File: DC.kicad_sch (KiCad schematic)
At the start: 52 parts, among them J1 348302001, J2 348302001, U6 MCP2551-I-P, U7 NUCLEO-F302R8

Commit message: Updated LEDs, buttons and power distribution headers
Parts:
- added D2: LTST-C193TBKT-5A, LTST-C193TBKT-5A:0603, symbol LTST-C193TBKT-5A:LTST-C193TBKT-5A
- added D3: LTW-C191DS5, LTW-C191DS5:LEDC1608X65N, symbol LTW-C191DS5:LTW-C191DS5
- added F10, F8, F9: 0466.125NR, FUSC3215X66N, symbol 0466_125NR:0466.125NR
- added LED1: LTST-C170GKT, LED_LTST-C170GKT_LTO, symbol 2026-02-10_18-36-51:LTST-C170GKT
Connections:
- net +12V: now also D2.2, D3.A, LED1.2
- net GND: now also U6.5 (Vref), F10.2, F8.2, F9.2
- new net: D3.C, F10.1
- new net: F8.1, LED1.1
- new net: D2.1, F9.1
- no-connect marks 43 -> 42
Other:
- moved on the sheet: J1, J2, a1, a2, a3, a4

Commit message: AccelIn to adc and I2C connection
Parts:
- removed R13: 3.3kΩ, DriverControlsLib:RES-TH_BD2.2-L6.5-P10.50-D0.6, symbol DC_Parts:R
- added D4, D5, D6, D7: LTST-C193TBKT-5A, LTST-C193TBKT-5A:0603, symbol LTST-C193TBKT-5A:LTST-C193TBKT-5A
- added F11, F12, F13, F14, F15, F16, F17, F18: 0466.125NR, FUSC3215X66N, symbol 0466_125NR:0466.125NR
- added J3: 757570141, CONN_SD-75757-010_1X4_F11p20_MOL, symbol 2026-02-11_03-05-32:757570141
- added LED2, LED3, LED4, LED5: LTST-C170GKT, LED_LTST-C170GKT_LTO, symbol 2026-02-10_18-36-51:LTST-C170GKT
- added R18: RC1206FR-07665RL, RC1206FR-07665RL:RESC3116X65N, symbol RC1206FR-07665RL:RC1206FR-07665RL
- added R19, R26, R27, R28, R29: RC1206FR-071K24L, RC1206FR-071K24L:RESC3116X65N, symbol RC1206FR-071K24L:RC1206FR-071K24L
- added R20, R22, R23, R24, R25: RC1206FR-072K32L, RC1206FR-072K32L:RESC3116X65N, symbol RC1206FR-072K32L:RC1206FR-072K32L
- added R21: RC1206FR-102K2L, RC1206FR-102K2L:RESC3116X65N, symbol RC1206FR-102K2L:RC1206FR-102K2L
- added S6, S7, S8, S9: LP6OA2ASRG, LP6OA2ASRG, symbol LP6OA2ASRG:LP6OA2ASRG
- R12: value 12kΩ -> 120Ω
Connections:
- net +12V: now also F10.1, F7.1, F8.1, F9.1, F11.1, F12.1, F13.1, F14.1, F15.1, F16.1, F17.1, F18.1, J3.1; no longer D1.A, D2.2, D3.A, LED1.2
- net +3.3V: now also S6.1, S7.1, S8.1, S9.1
- net AccelIn: now also U7.CN7_28 (PA0); no longer U7.CN10_23 (PA8)
- net CAN_H: now also J3.2
- net CAN_L: now also J3.3
- net GND: now also D1.C, D2.1, D3.C, LED1.1, R12.1, D4.1, D5.1, D6.1, D7.1, J3.4, LED2.1, LED3.1, LED4.1, LED5.1; no longer F10.2, F7.2, F8.2, F9.2, U6.5 (Vref), U6.8 (Rs)
- net SupBattery: no longer R12.1
- net To_PreChargeBtn: now also S4.3; no longer S4.2
- net I2C1_SDA: now reaches U7.CN10_1 (PC9)
- net I2C1_CLK: now reaches U7.CN10_3 (PB8)
- net SupBattMonitor: no longer names the net of R12.2
- net SupBattMonitor: now also U6.8 (Rs); no longer U7.CN10_22 (PB2)
- new net: F10.2, R21.1
- new net: F11.2, R22.1
- new net: D4.2, R22.2
- new net: D3.A, R21.2
- new net: F8.2, R19.1
- new net: F14.2, R25.1
- new net: D7.2, R25.2
- new net: F18.2, R29.1
- new net: F12.2, R23.1
- new net: F15.2, R26.1
- new net: LED2.2, R26.2
- new net: LED1.2, R19.2
- new net: F17.2, R28.1
- new net: LED4.2, R28.2
- new net: D1.A, R18.2
- new net: F7.2, R18.1
- new net: F13.2, R24.1
- new net: D6.2, R24.2
- new net: LED5.2, R29.2
- new net: F16.2, R27.1
- new net: LED3.2, R27.2
- new net: D5.2, R23.2
- new net: F9.2, R20.1
- new net: D2.2, R20.2
- new net SolarBtn: S6.3, S7.3, S8.3, S9.3
- no-connect marks 42 -> 39
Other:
- note removed: "Supplemental Battery Monitor"
- moved on the sheet: C10, C7, C8, C9, D1, D2, D3, F1, F10, F2, F3, F4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

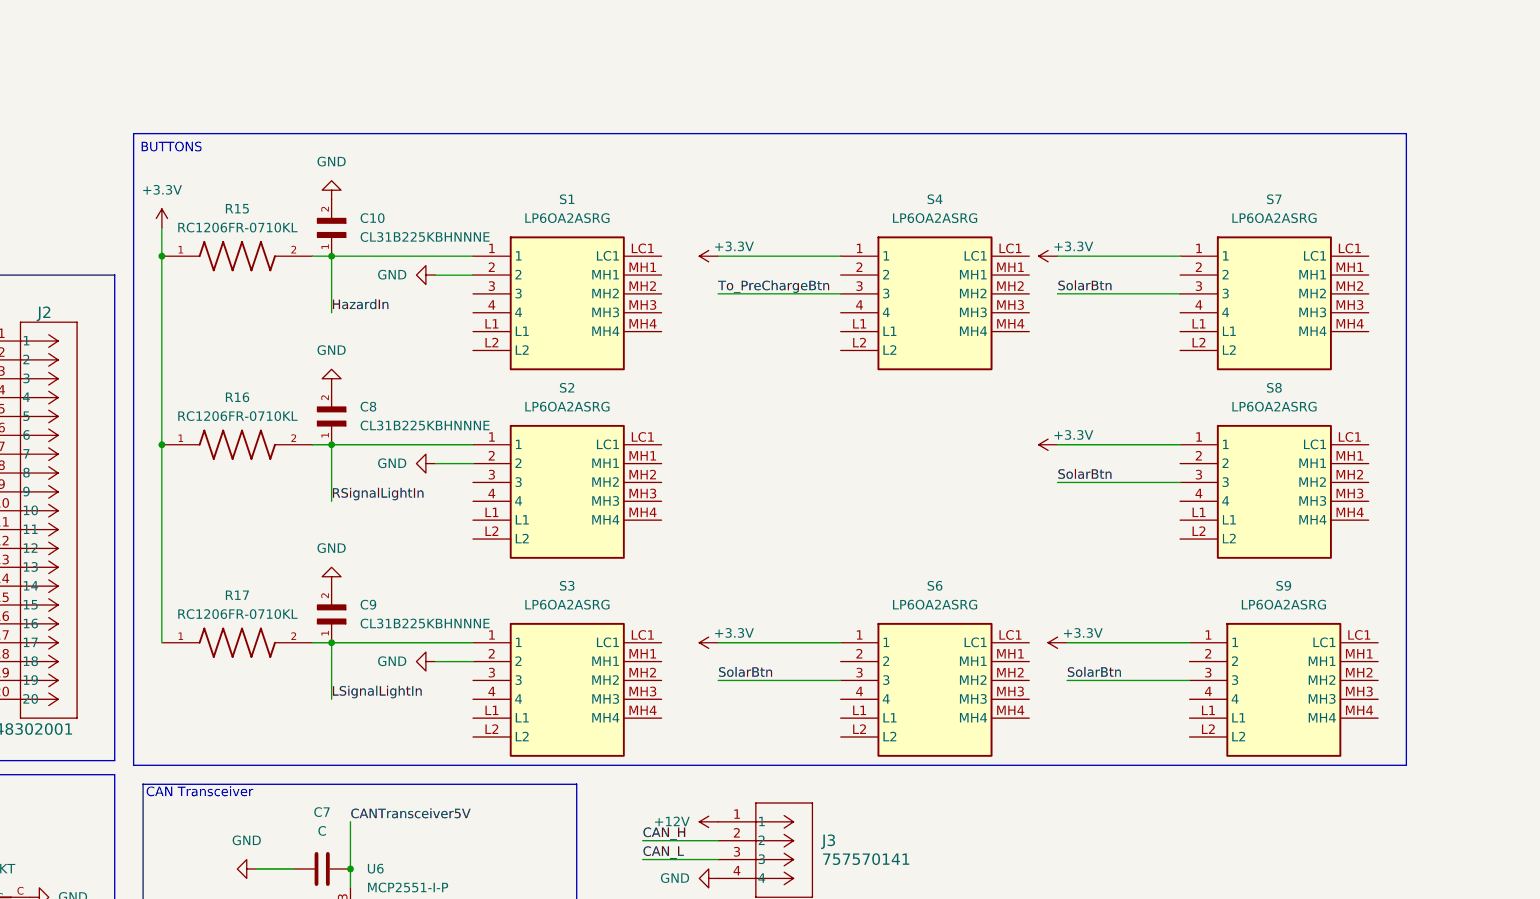
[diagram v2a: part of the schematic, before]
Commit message: Deleted buttons!
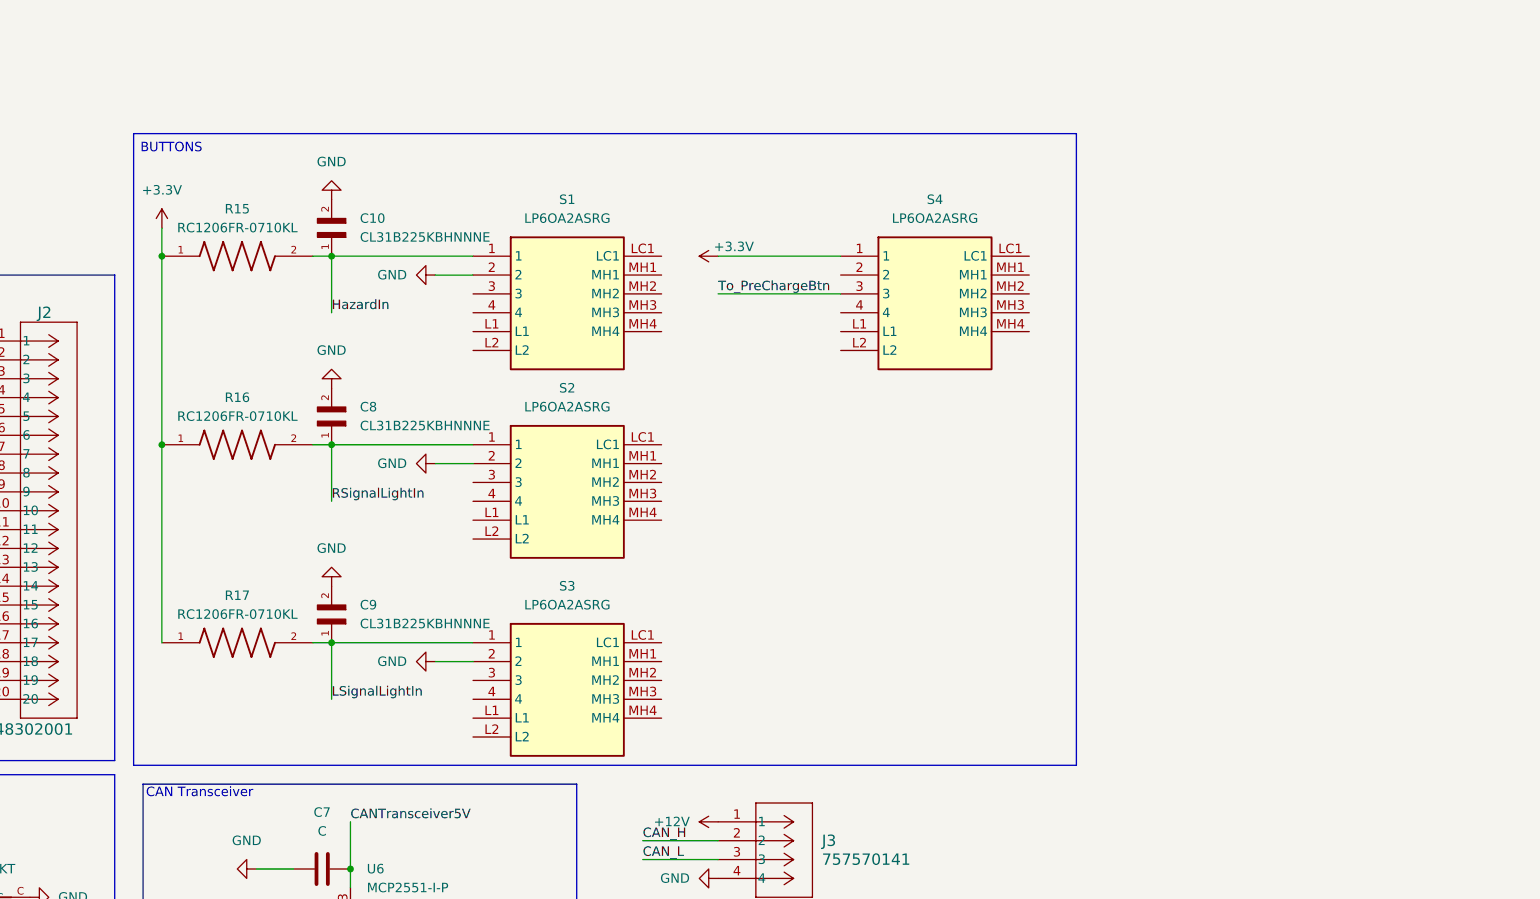
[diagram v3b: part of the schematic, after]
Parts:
- removed S6, S7, S8, S9: LP6OA2ASRG, LP6OA2ASRG, symbol LP6OA2ASRG:LP6OA2ASRG

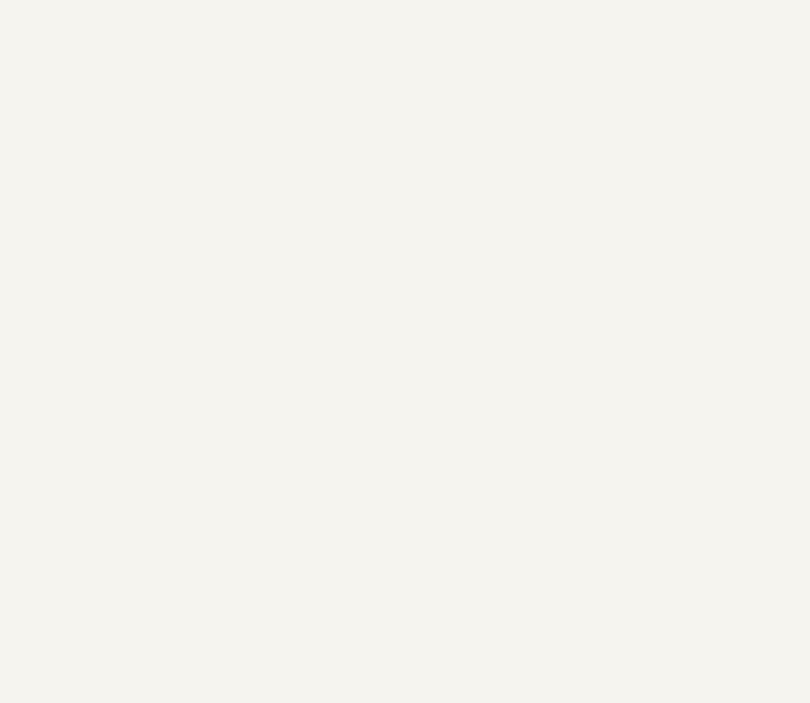
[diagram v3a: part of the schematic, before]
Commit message: Added LCD!
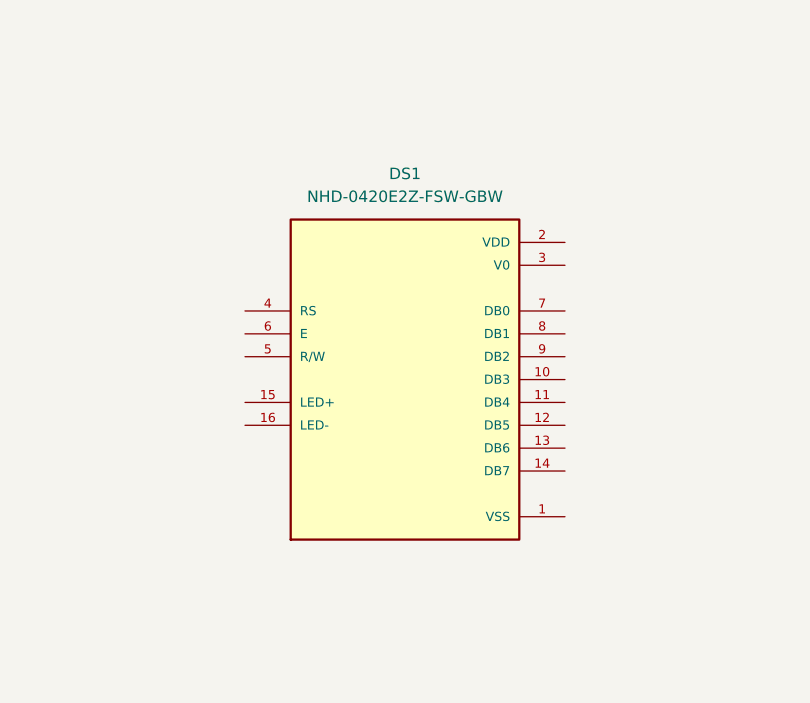
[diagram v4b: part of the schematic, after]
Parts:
- added DS1: NHD-0420E2Z-FSW-GBW, NHD-0420E2Z-FSW-GBW:LCD_NHD-0420E2Z-FSW-GBW, symbol NHD-0420E2Z-FSW-GBW:NHD-0420E2Z-FSW-GBW
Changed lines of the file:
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@@
+	)
+	(symbol
+		(lib_id "NHD-0420E2Z-FSW-GBW:NHD-0420E2Z-FSW-GBW")
+		(at 229.87 167.64 0)
+		(unit 1)
+		(exclude_from_sim no)
+		(in_bom yes)
+		(on_board yes)
+		(dnp no)
+		(fields_autoplaced yes)
+		(property "Reference" "DS1"
+			(at 229.87 144.78 0)
+			(effects
+				(font
+					(size 1.27 1.27)
+				)
+			)
+		)
+		(property "Value" "NHD-0420E2Z-FSW-GBW"
+			(at 229.87 147.32 0)
+			(effects
+				(font
+					(size 1.27 1.27)
+				)
+			)
+		)
+		(property "Footprint" "NHD-0420E2Z-FSW-GBW:LCD_NHD-0420E2Z-FSW-GBW"
+			(at 229.87 167.64 0)
+			(effects
+				(font
+					(size 1.27 1.27)
+				)
+				(justify bottom)
+				(hide yes)
+			)
+		)
+		(property "Datasheet" ""
+			(at 229.87 167.64 0)
+			(effects
+				(font
+					(size 1.27 1.27)
+				)
+				(hide yes)
+			)
+		)
+		(property "Description" ""
+			(at 229.87 167.64 0)
+			(effects
+				(font
+					(size 1.27 1.27)
+				)
+				(hide yes)
+			)
+		)
+		(property "MAXIMUM_PACKAGE_HEIGHT" "14.5mm"
+			(at 229.87 167.64 0)
+			(effects
+				(font
+					(size 1.27 1.27)
+				)
+				(justify bottom)
+				(hide yes)
+			)
+		)
+		(property "CREATOR" "ANA"
+			(at 229.87 167.64 0)
+			(effects
+				(font
+					(size 1.27 1.27)
+				)
+				(justify bottom)
+				(hide yes)
+			)
+		)
+		(property "STANDARD" "IPC-7351B"
+			(at 229.87 167.64 0)
+			(effects
+				(font
+					(size 1.27 1.27)
+				)
+				(justify bottom)
+				(hide yes)
+			)
+		)
+		(property "PARTREV" "4"
+			(at 229.87 167.64 0)
+			(effects
+				(font
+					(size 1.27 1.27)
+				)
+				(justify bottom)
+				(hide yes)
+			)
+		)
+		(property "VERIFIER" "RODRIGO"
+			(at 229.87 167.64 0)
+			(effects
+				(font
+					(size 1.27 1.27)
+				)
+				(justify bottom)
+				(hide yes)
+			)
+		)
+		(property "MANUFACTURER" "Newhaven Display Intl"
+			(at 229.87 167.64 0)
+			(effects
+				(font
+					(size 1.27 1.27)
+				)
+				(justify bottom)
+				(hide yes)
+			)
+		)
+		(pin "2"
+		)
+		(pin "7"
+		)
+		(pin "1"
+		)
+		(pin "11"
+		)
+		(pin "3"
+		)
+		(pin "5"
+		)
+		(pin "9"
+		)
+		(pin "12"
+		)
+		(pin "16"
+		)
+		(pin "10"
+		)
+		(pin "13"
+		)
+		(pin "4"
+		)
+		(pin "6"
+		)
+		(pin "15"
+		)
+		(pin "8"
+		)
+		(pin "14"
+		)
+		(instances
+			(project ""
+				(path "/7c560bbd-cfc0-42ab-b727-e631475cbcaa"
+					(reference "DS1")
+					(unit 1)
+				)
+			)
+		)
 	)
 	(symbol

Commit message: Added LCD!
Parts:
- DS1: footprint NHD-0420E2Z-FSW-GBW:LCD_NHD-0420E2Z-FSW-GBW -> MiscellaneousLibrary:LCD_NHD-0420E2Z-FSW-GBW
- F10, F11, F12, F13, F14, F15, F16, F17, F18, F7, F8, F9: footprint FUSC3215X66N -> (none)
- J1, J2: footprint CONN_SD-34829-001_20_ST_MOL -> (none)
- J3: footprint CONN_SD-75757-010_1X4_F11p20_MOL -> (none)
- LED1, LED2, LED3, LED4, LED5: footprint LED_LTST-C170GKT_LTO -> (none)
- S1, S2, S3, S4: footprint LP6OA2ASRG -> (none)
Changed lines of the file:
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@@
 			)
 		)
-		(property "Footprint" "FUSC3215X66N"
+		(property "Footprint" ""
 			(at 40.64 375.59 0)
 			(effects
@@
 			)
 		)
-		(property "Footprint" "NHD-0420E2Z-FSW-GBW:LCD_NHD-0420E2Z-FSW-GBW"
+		(property "Footprint" "MiscellaneousLibrary:LCD_NHD-0420E2Z-FSW-GBW"
 			(at 229.87 167.64 0)
 			(effects
@@
 			)
 		)
-		(property "Footprint" "FUSC3215X66N"
+		(property "Footprint" ""
 			(at 40.64 235.89 0)
 			(effects
@@
 			)
 		)
-		(property "Footprint" "CONN_SD-34829-001_20_ST_MOL"
+		(property "Footprint" ""
 			(at 35.56 48.26 0)
 			(effects
@@
 			)
 		)
-		(property "Footprint" "FUSC3215X66N"
+		(property "Footprint" ""
 			(at 40.64 293.04 0)
 			(effects
@@
 			)
 		)
-		(property "Footprint" "FUSC3215X66N"
+		(property "Footprint" ""
 			(at 40.64 333.68 0)
 			(effects
@@
 			)
 		)
-		(property "Footprint" "FUSC3215X66N"
+		(property "Footprint" ""
 			(at 40.64 322.25 0)
 			(effects
@@
 			)
 		)
-		(property "Footprint" "CONN_SD-34829-001_20_ST_MOL"
+		(property "Footprint" ""
 			(at 76.2 48.26 0)
 			(effects
@@
 			)
 		)
-		(property "Footprint" "LED_LTST-C170GKT_LTO"
+		(property "Footprint" ""
 			(at 68.58 181.61 0)
 			(effects
@@
 			)
 		)
-		(property "Footprint" "FUSC3215X66N"
+		(property "Footprint" ""
 			(at 40.64 277.8 0)
 			(effects
@@
 			)
 		)
-		(property "Footprint" "FUSC3215X66N"
+		(property "Footprint" ""
 			(at 40.64 219.38 0)
 			(effects
@@
 			)
 		)
-		(property "Footprint" "LP6OA2ASRG"
+		(property "Footprint" ""
 			(at 213.36 131.75 0)
 			(effects
@@
 			)
 		)
-		(property "Footprint" "LP6OA2ASRG"
+		(property "Footprint" ""
 			(at 163.83 157.15 0)
 			(effects
@@
 			)
 		)
-		(property "Footprint" "LP6OA2ASRG"
+		(property "Footprint" ""
 			(at 163.83 131.75 0)
 			(effects
@@
 			)
 		)
-		(property "Footprint" "LED_LTST-C170GKT_LTO"
+		(property "Footprint" ""
 			(at 68.58 196.85 0)
 			(effects
@@
 			)
 		)
-		(property "Footprint" "LED_LTST-C170GKT_LTO"
+		(property "Footprint" ""
 			(at 68.58 153.67 0)
 			(effects
@@
 			)
 		)
-		(property "Footprint" "CONN_SD-75757-010_1X4_F11p20_MOL"
+		(property "Footprint" ""
 			(at 175.26 113.03 0)
 			(effects
@@
 			)
 		)
-		(property "Footprint" "FUSC3215X66N"
+		(property "Footprint" ""
 			(at 40.64 346.38 0)
 			(effects
@@
 			)
 		)
-		(property "Footprint" "LED_LTST-C170GKT_LTO"
+		(property "Footprint" ""
 			(at 68.58 167.64 0)
 			(effects
@@
 			)
 		)
-		(property "Footprint" "LP6OA2ASRG"
+		(property "Footprint" ""
 			(at 163.83 183.82 0)
 			(effects
@@
 			)
 		)
-		(property "Footprint" "FUSC3215X66N"
+		(property "Footprint" ""
 			(at 40.64 249.86 0)
 			(effects
@@
 			)
 		)
-		(property "Footprint" "FUSC3215X66N"
+		(property "Footprint" ""
 			(at 40.64 357.81 0)
 			(effects
@@
 			)
 		)
-		(property "Footprint" "FUSC3215X66N"
+		(property "Footprint" ""
 			(at 40.64 263.83 0)
 			(effects
@@
 			)
 		)
-		(property "Footprint" "LED_LTST-C170GKT_LTO"
+		(property "Footprint" ""
 			(at 68.58 139.7 0)
 			(effects
@@
 			)
 		)
-		(property "Footprint" "FUSC3215X66N"
+		(property "Footprint" ""
 			(at 40.64 310.82 0)
 			(effects
